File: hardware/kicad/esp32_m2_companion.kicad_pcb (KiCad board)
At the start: 4 copper layers, 22 x 42 mm, 33 parts, among them J1 M2_KEYB_2242_EDGE, J3 Conn_01x04, J4 Conn_01x08, U1 USBLC6-2SC6, U2 ESP32-S3-WROOM-1

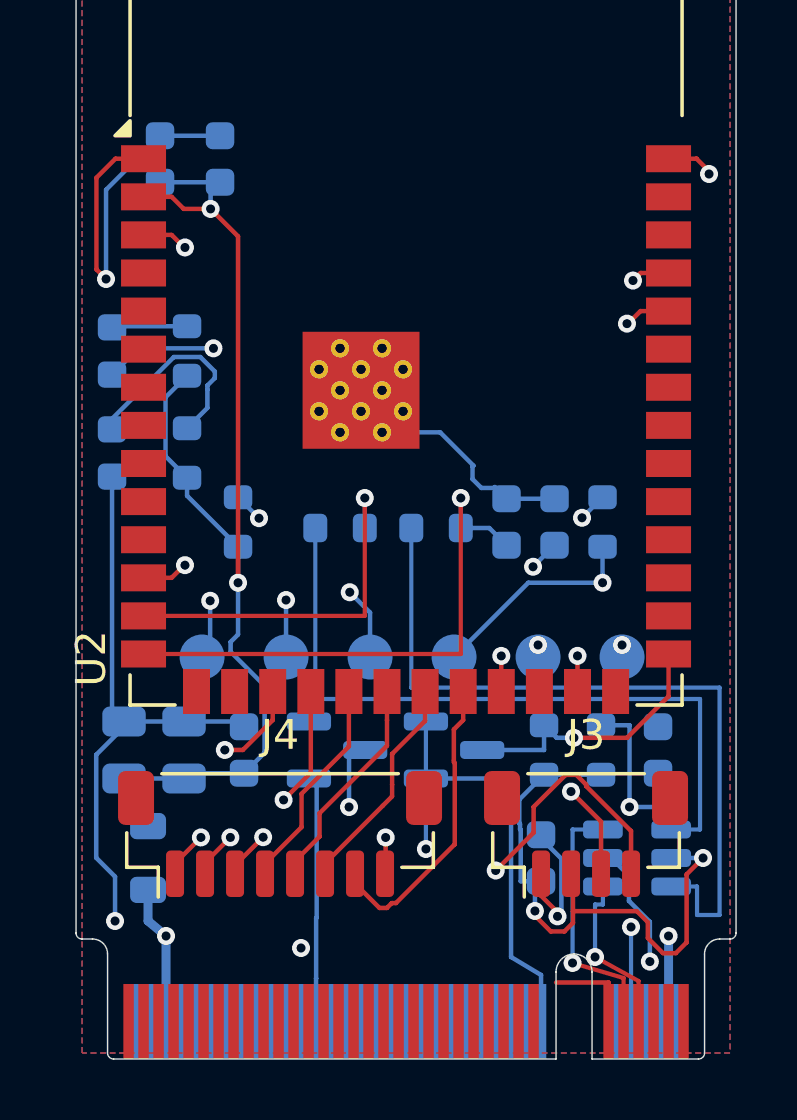
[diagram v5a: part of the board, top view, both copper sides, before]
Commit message: Phase 2 routing: clean base, USB pair intact, 27/28 nets (W_DISABLE1_n for GUI)
- reverted the D+ fan-west experiment that broke the USB pair; USB pair
  back to known-good 90ohm route
- 27/28 nets routed, DRC clean of real shorts (3 benign J1 artifacts only)
- W_DISABLE1_n (secondary BOOT strap) left as one interactive track;
  method + waypoints in docs/routing-status.md
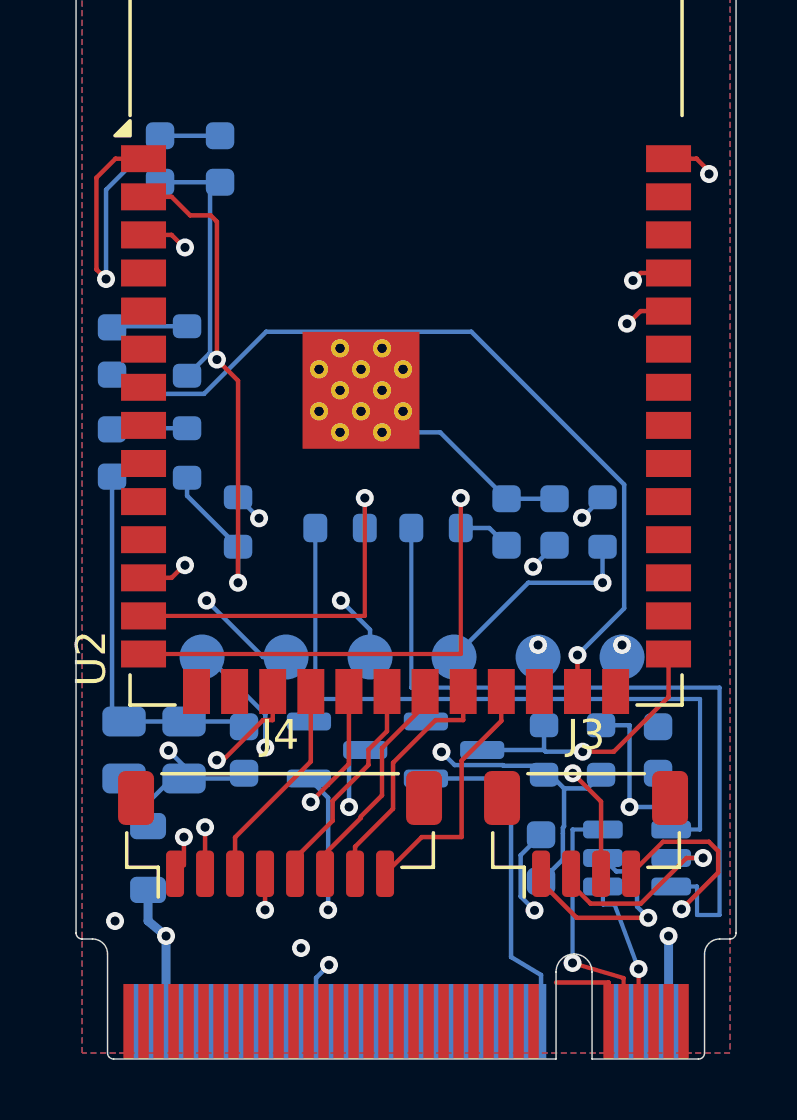
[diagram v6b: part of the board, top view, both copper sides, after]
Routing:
- net GND: track 138.3 -> 108.7 mm, vias 19 -> 18
- net W_DISABLE1_n: track 16.8 -> 0.00 mm, vias 2 -> 0
- net IO9: track 31.4 -> 36.8 mm
- net +3V3_M2: track 27.4 -> 32.1 mm, vias 2 -> 3
- net N$1: track 7.11 -> 2.52 mm
- net IO11: track 7.23 -> 9.64 mm, vias 0 -> 2
- net IO0_BOOT: track 26.7 -> 24.3 mm
- net RXD0: track 33.5 -> 31.5 mm
- net IO14: track 10.1 -> 8.11 mm
- net +3V3: track 89.4 -> 91.4 mm, vias 5 -> 6
- net IO21: track 10.1 -> 8.46 mm, vias 2 -> 0
- net TXD0: track 36.3 -> 35.6 mm
- net USBH3_D_P: track 5.62 -> 5.03 mm
- net PERST_n: track 8.21 -> 8.56 mm, vias 0 -> 2
- net LED_STATUS_n: track 27.9 -> 27.8 mm, vias 2 -> 1
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
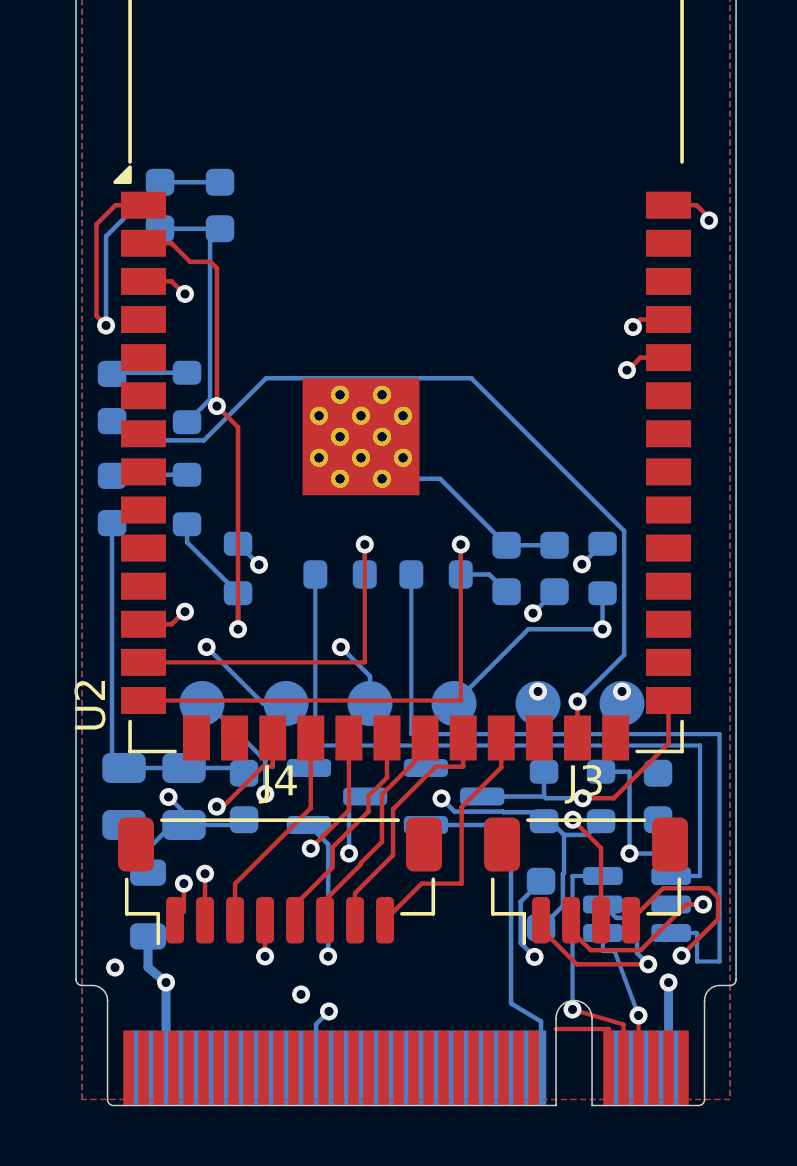
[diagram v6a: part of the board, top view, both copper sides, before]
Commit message: Board fully routed (all signal nets) + pin-8 (W_DISABLE1_n) dropped in v1
ROUTING: root cause of the multi-run saga was too few freerouting passes
(cut to 6 for speed; hard recovery nets need ~50+). Restored to 80 passes ->
all 27 signal nets route, USB 90ohm pair hand-locked, 4 planes poured, EPAD
via grid. DRC: no real shorts; residual = GND zone-island + 3 J1
footprint-internal notes (all benign).

PIN 8 DROP (ADR 0002 amendment): W_DISABLE1_n BOOT leg removed - unroutable
in the pin 7/8/9 interleave AND redundant with TP1(EN)+TP2(BOOT) flying-lead
recovery. D2 pin 2 = NC; edge finger exposed/unconnected. Mallow recovery
(pin 50 + pin 20) intact.

Regenerated from sources: schematic PDF, DATASHEET.md, pinmap, 3D
(GLB/STEP/STL/viewer), board renders. Docs: ADR 0002, risks (R10/R10b),
findings, sideband_recovery LESSONS.
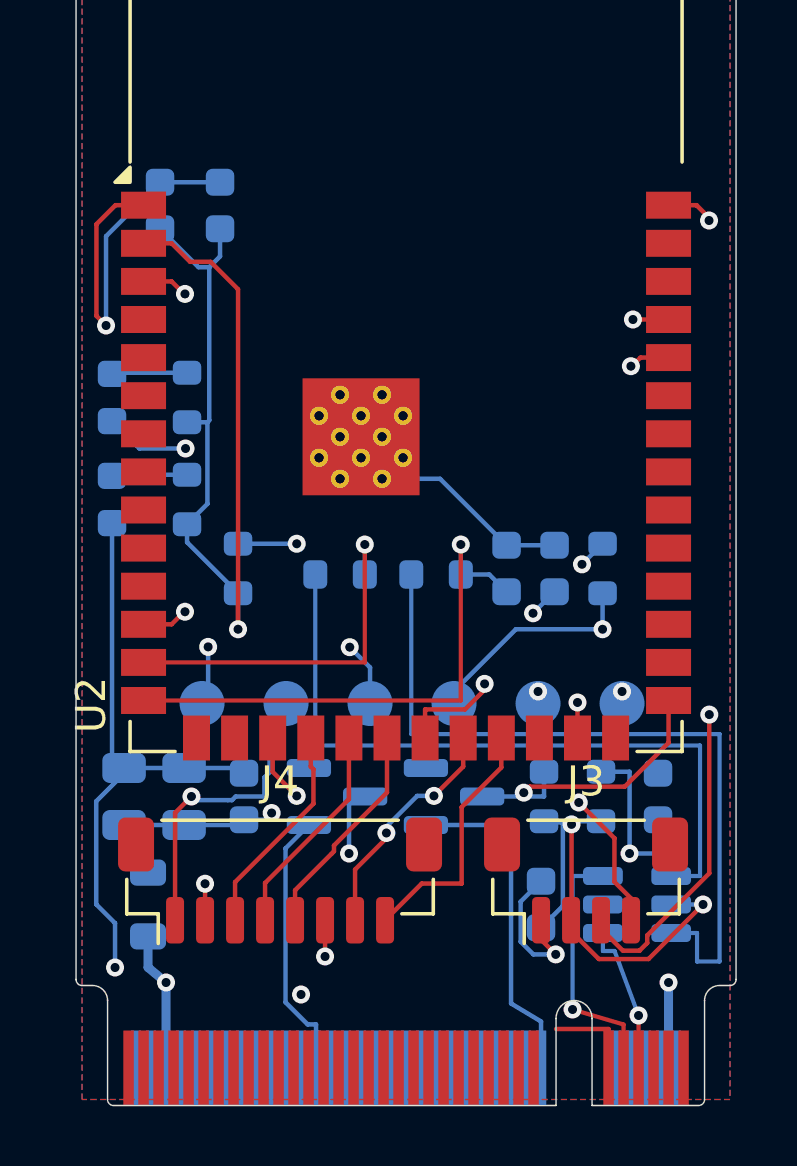
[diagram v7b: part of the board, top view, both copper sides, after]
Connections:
- D2 pad 2: W_DISABLE1_n -> (no net)
- J1 pad 8: W_DISABLE1_n -> (no net)
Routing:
- net GND: track 108.7 -> 128.9 mm, vias 18 -> 17
- net IO8: track 30.5 -> 42.2 mm
- net IO9: track 36.8 -> 27.3 mm
- net TXD0: track 35.6 -> 44.5 mm, vias 3 -> 2
- net IO13: track 7.46 -> 15.9 mm, vias 0 -> 2
- net LED_STATUS_n: track 27.8 -> 22.1 mm, vias 1 -> 2
- net +3V3: track 91.4 -> 95.2 mm, vias 6 -> 5
- net IO0_BOOT: track 24.3 -> 27.7 mm
- net EN: track 46.0 -> 49.1 mm
- net IO11: track 9.64 -> 7.23 mm, vias 2 -> 0
- net RXD0: track 31.5 -> 30.6 mm
- net PERST_n: track 8.56 -> 9.01 mm, vias 2 -> 0
- net IO14: track 8.11 -> 7.89 mm, vias 0 -> 2
